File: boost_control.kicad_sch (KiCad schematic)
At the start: 5 parts, among them U2 AD5259BRMZ100

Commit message: Working on layout for dev board
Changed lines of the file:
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@@
 	)
 	(bus_entry
-		(at 74.93 100.33)
-		(size 2.54 -2.54)
+		(at 195.58 80.01)
+		(size -2.54 -2.54)
 		(stroke
 			(width 0)
@@
 	(wire
 		(pts
-			(xy 189.23 77.47) (xy 187.96 77.47)
+			(xy 187.96 77.47) (xy 193.04 77.47)
 		)
 		(stroke
@@
 	(bus
 		(pts
-			(xy 68.58 105.41) (xy 74.93 105.41)
+			(xy 200.66 82.55) (xy 195.58 82.55)
 		)
 		(stroke
@@
 	(bus
 		(pts
-			(xy 74.93 100.33) (xy 74.93 105.41)
+			(xy 195.58 80.01) (xy 195.58 82.55)
 		)
 		(stroke
@@
 			(width 0)
 			(type default)
-		)
-	)
-	(wire
-		(pts
-			(xy 77.47 97.79) (xy 81.28 97.79)
-		)
-		(stroke
-			(width 0)
-			(type default)
-		)
-	)
-	(label "FB"
-		(at 81.28 97.79 180)
-		(effects
-			(font
-				(size 1.27 1.27)
-			)
-			(justify right bottom)
 		)
 	)
@@
 	(hierarchical_label "{SIG_BOOST}"
 		(shape bidirectional)
-		(at 68.58 105.41 180)
+		(at 200.66 82.55 0)
 		(effects
 			(font
 				(size 1.27 1.27)
 			)
-			(justify right)
-		)
-	)
+			(justify left)
+		)
+	)

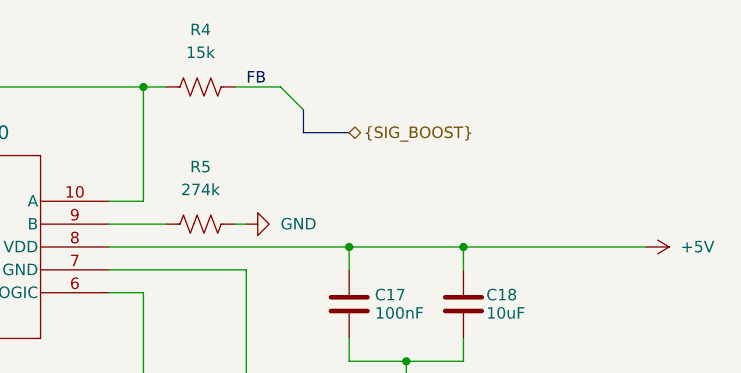
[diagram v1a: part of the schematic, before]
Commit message: Working on layout. Adding in TPs to schematic
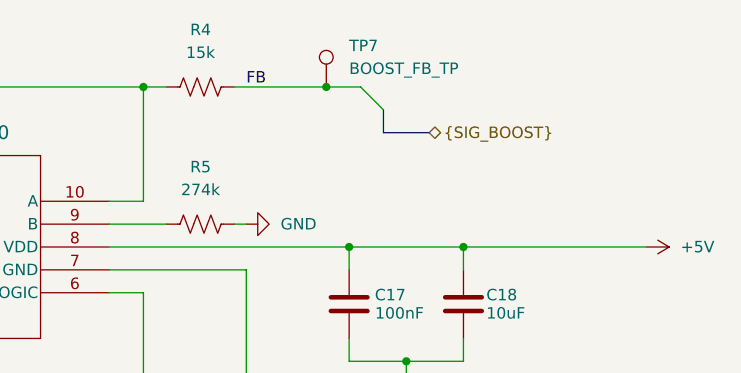
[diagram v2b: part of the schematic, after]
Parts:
- added TP7: BOOST_FB_TP, symbol Connector:TestPoint
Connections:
- net FB: now also TP7.1
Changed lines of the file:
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@@
+	)
+	(junction
+		(at 198.12 77.47)
+		(diameter 0)
+		(color 0 0 0 0)
 	)
 	(junction
@@
 	)
 	(bus_entry
-		(at 195.58 80.01)
+		(at 204.47 80.01)
 		(size -2.54 -2.54)
 		(stroke
@@
 	(wire
 		(pts
-			(xy 187.96 77.47) (xy 193.04 77.47)
+			(xy 187.96 77.47) (xy 198.12 77.47)
 		)
 		(stroke
@@
 	(bus
 		(pts
-			(xy 200.66 82.55) (xy 195.58 82.55)
+			(xy 209.55 82.55) (xy 204.47 82.55)
 		)
 		(stroke
@@
 	(wire
 		(pts
+			(xy 198.12 77.47) (xy 201.93 77.47)
+		)
+		(stroke
+			(width 0)
+			(type default)
+		)
+	)
+	(wire
+		(pts
 			(xy 173.99 100.33) (xy 177.8 100.33)
 		)
@@
 	(bus
 		(pts
-			(xy 195.58 80.01) (xy 195.58 82.55)
+			(xy 204.47 80.01) (xy 204.47 82.55)
 		)
 		(stroke
@@
 	(hierarchical_label "{SIG_BOOST}"
 		(shape bidirectional)
-		(at 200.66 82.55 0)
+		(at 209.55 82.55 0)
 		(effects
 			(font
@@
 					(unit 1)
 				)
+			)
+		)
+	)
+	(symbol
+		(lib_id "Connector:TestPoint")
+		(at 198.12 77.47 0)
+		(unit 1)
+		(exclude_from_sim no)
+		(in_bom yes)
+		(on_board yes)
+		(dnp no)
+		(fields_autoplaced yes)
+		(property "Reference" "TP7"
+			(at 200.66 72.8979 0)
+			(effects
+				(font
+					(size 1.27 1.27)
+				)
+				(justify left)
+			)
+		)
+		(property "Value" "BOOST_FB_TP"
+			(at 200.66 75.4379 0)
+			(effects
+				(font
+					(size 1.27 1.27)
+				)
+				(justify left)
+			)
+		)
+		(property "Footprint" ""
+			(at 203.2 77.47 0)
+			(effects
+				(font
+					(size 1.27 1.27)
+				)
+				(hide yes)
+			)
+		)
+		(property "Datasheet" "~"
+			(at 203.2 77.47 0)
+			(effects
+				(font
+					(size 1.27 1.27)
+				)
+				(hide yes)
+			)
+		)
+		(property "Description" "test point"
+			(at 198.12 77.47 0)
+			(effects
+				(font
+					(size 1.27 1.27)
+				)
+				(hide yes)
+			)
+		)
+		(property "Mfr" ""
+			(at 198.12 77.47 0)
+			(effects
+				(font
+					(size 1.27 1.27)
+				)
+				(hide yes)
+			)
+		)
+		(property "Mfr P/N" ""
+			(at 198.12 77.47 0)
+			(effects
+				(font
+					(size 1.27 1.27)
+				)
+				(hide yes)
+			)
+		)
+		(property "Supplier_1" ""
+			(at 198.12 77.47 0)
+			(effects
+				(font
+					(size 1.27 1.27)
+				)
+				(hide yes)
+			)
+		)
+		(property "Supplier_1 P/N" ""
+			(at 198.12 77.47 0)
+			(effects
+				(font
+					(size 1.27 1.27)
+				)
+				(hide yes)
+			)
+		)
+		(property "Supplier_1 Unit Price" ""
+			(at 198.12 77.47 0)
+			(effects
+				(font
+					(size 1.27 1.27)
+				)
+				(hide yes)
+			)
+		)
+		(property "Supplier_1 Price @ Qty" ""
+			(at 198.12 77.47 0)
+			(effects
+				(font
+					(size 1.27 1.27)
+				)
+				(hide yes)
+			)
+		)
+		(property "Supplier_2" ""
+			(at 198.12 77.47 0)
+			(effects
+				(font
+					(size 1.27 1.27)
+				)
+				(hide yes)
+			)
+		)
+		(property "Supplier_2 P/N" ""
+			(at 198.12 77.47 0)
+			(effects
+				(font
+					(size 1.27 1.27)
+				)
+				(hide yes)
+			)
+		)
+		(property "Supplier_2 Unit Price" ""
+			(at 198.12 77.47 0)
+			(effects
+				(font
+					(size 1.27 1.27)
+				)
+				(hide yes)
+			)
+		)
+		(property "Supplier_2 Price @ Qty" ""
+			(at 198.12 77.47 0)
+			(effects
+				(font
+					(size 1.27 1.27)
+				)
+				(hide yes)
+			)
+		)
+		(pin "1"
+		)
+		(instances
+			(project ""
+				(path "/99785679-20de-4827-b4cc-bc3c187068c9/9564929a-642e-4163-88c2-45054b63a5ed/09b4163a-819e-413e-b808-030375832f4a"
+					(reference "TP7")
+					(unit 1)
+				)
+				(path "/99785679-20de-4827-b4cc-bc3c187068c9/9564929a-642e-4163-88c2-45054b63a5ed/84126d6b-9224-455f-9cea-3582a8eebe20"
+					(reference "TP8")
+					(unit 1)
+				)

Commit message: Working on tp
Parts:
- renumbered TP7 to TP1
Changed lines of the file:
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@@
 		(dnp no)
 		(fields_autoplaced yes)
-		(property "Reference" "TP7"
+		(property "Reference" "TP1"
 			(at 200.66 72.8979 0)
 			(effects
@@
 			(project ""
 				(path "/99785679-20de-4827-b4cc-bc3c187068c9/9564929a-642e-4163-88c2-45054b63a5ed/09b4163a-819e-413e-b808-030375832f4a"
-					(reference "TP7")
+					(reference "TP1")
 					(unit 1)
 				)
 				(path "/99785679-20de-4827-b4cc-bc3c187068c9/9564929a-642e-4163-88c2-45054b63a5ed/84126d6b-9224-455f-9cea-3582a8eebe20"
-					(reference "TP8")
+					(reference "TP4")
 					(unit 1)
 				)
